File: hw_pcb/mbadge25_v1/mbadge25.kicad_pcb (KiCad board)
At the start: 2 copper layers, 8 parts, among them J1 USB4105-GF-A, U1 ESP32-C3-MINI-1

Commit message: v1 draft PCB layout
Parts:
- added C3: 100nF, Library_FP_mbadge25:C_1206_3216Metric_Pad1.33x1.80mm, F.Cu at (112.5, 83.2)
- added C4: 2.2µF, Library_FP_mbadge25:C_1206_3216Metric_Pad1.33x1.80mm, F.Cu at (103.2, 76.0)
- added C5: 2.2µF, Library_FP_mbadge25:C_1206_3216Metric_Pad1.33x1.80mm, F.Cu at (103.2, 78.8)
- added C6: 2.2µF, Library_FP_mbadge25:C_1206_3216Metric_Pad1.33x1.80mm, F.Cu at (112.7, 76.5)
- added C7: 100nF, Library_FP_mbadge25:C_1206_3216Metric_Pad1.33x1.80mm, F.Cu at (122.5, 86.5)
- added C8: 1µF, Library_FP_mbadge25:C_1206_3216Metric_Pad1.33x1.80mm, F.Cu at (77.5, 86.5)
- added C9: 1µF, Library_FP_mbadge25:C_1206_3216Metric_Pad1.33x1.80mm, F.Cu at (99.8, 88.5)
- added J2: BAT, Library_FP_mbadge25:PinHeader_1x02_P2.54mm_Vertical, F.Cu at (79.7, 53.0)
- added J3: OLED_I2C, Library_FP_mbadge25:OLED_128x32, F.Cu at (100.0, 82.0)
- added J4: BAT, Library_FP_mbadge25:Pad_6.0mm_Drill3.0mm, F.Cu at (76.0, 48.0)
- added J5: GND, Library_FP_mbadge25:Pad_6.0mm_Drill3.0mm, F.Cu at (124.0, 48.0)
- added J6: BAT, Library_FP_mbadge25:Pad_1.2mm_Drill0.7mm, F.Cu at (76.0, 53.0)
- added J7: GND, Library_FP_mbadge25:Pad_1.2mm_Drill0.7mm, F.Cu at (124.0, 53.0)
- added R2: 5k1, Library_FP_mbadge25:R_1206_3216Metric_Pad1.30x1.75mm, F.Cu at (116.0, 88.5)
- added R3: 27E, Library_FP_mbadge25:R_1206_3216Metric_Pad1.30x1.75mm, F.Cu at (108.0, 88.5)
- added R4: 27E, Library_FP_mbadge25:R_1206_3216Metric_Pad1.30x1.75mm, F.Cu at (110.5, 88.5)
- added R5: 100k, Library_FP_mbadge25:R_1206_3216Metric_Pad1.30x1.75mm, F.Cu at (112.5, 80.5)
- added R6: 100k, Library_FP_mbadge25:R_1206_3216Metric_Pad1.30x1.75mm, F.Cu at (122.5, 83.8)
- added R7: 10k, Library_FP_mbadge25:R_1206_3216Metric_Pad1.30x1.75mm, F.Cu at (77.5, 83.8)
- added R8: 220E, Library_FP_mbadge25:R_1206_3216Metric_Pad1.30x1.75mm, F.Cu at (122.5, 81.0)
- added S2: RST, Library_FP_mbadge25:SW_SPST, F.Cu at (77.5, 94.0)
- added T1: LP0404N3T5G, Library_FP_mbadge25:SOT-23-3, F.Cu at (103.5, 82.5)
- added U2: XC6220B331MR, Library_FP_mbadge25:SOT-23-5_HandSoldering, F.Cu at (108.7, 77.2)
- C1: value C -> 47pF; footprint PCM_Capacitor_SMD_AKL:C_0805_2012Metric_Pad1.18x1.45mm_HandSolder -> Library_FP_mbadge25:C_1206_3216Metric_Pad1.33x1.80mm
- C2: value C-polar -> 47pF; footprint PCM_Capacitor_SMD_AKL:CP_Elec_6.3x5.9 -> Library_FP_mbadge25:C_1206_3216Metric_Pad1.33x1.80mm
- D1: value type="" model="D" lib="semiconductor.lib" -> MSK4005; footprint Diode_SMD:D_SOD-123 -> Library_FP_mbadge25:D_SOD-523
- D2: value type="" model="D-LED" lib="semiconductor.lib" -> WS2812B; footprint Diode_SMD:D_SMA -> Library_FP_mbadge25:LED_WS2812B_PLCC4_5.0x5.0mm_P3.2mm
- R1: value R -> 5k1; footprint Resistor_SMD:R_0805_2012Metric -> Library_FP_mbadge25:R_1206_3216Metric_Pad1.30x1.75mm
- S1: value S-make-push -> SW; footprint Button_Switch_THT:SW_PUSH_6mm -> Library_FP_mbadge25:SW_SPST
- U1: footprint PCM_Espressif:ESP32-C3-MINI-1 -> Library_FP_mbadge25:ESP32-C3-MINI-1
- moved S1 86.3 mm to (122.5, 94.0), turned to 90 degrees
- moved J1 78.0 mm to (109.2, 97.2)
- moved C2 71.9 mm to (105.2, 88.5), turned to -90 degrees
- moved D2 70.6 mm to (122.5, 76.0), turned to -90 degrees
- moved U1 69.6 mm to (91.1, 91.5), turned to 180 degrees
- moved C1 66.2 mm to (113.2, 88.5), turned to -90 degrees
- moved D1 58.9 mm to (108.0, 80.8)
- moved R1 54.8 mm to (102.5, 88.5), turned to 90 degrees
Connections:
- C1 pad 1: unconnected-(C1-+-Pad1) -> /IO18.USBN
- C1 pad 2: unconnected-(C1---Pad2) -> /GND
- C2 pad 1: unconnected-(C2-+-Pad1) -> /IO19.USBP
- C2 pad 2: unconnected-(C2---Pad2) -> /GND
- D1 pad 1: unconnected-(D1-K--Pad1) -> /5V0
- D1 pad 2: unconnected-(D1-A+-Pad2) -> /VUSB
- D2 pad 1: unconnected-(D2-K--Pad1) -> /5V0
- D2 pad 2: unconnected-(D2-A+-Pad2) -> /RGB.DO
- J1 pad A1_B12: unconnected-(J1-GND-PadA1_B12) -> /GND
- J1 pad A4_B9: unconnected-(J1-VBUS-PadA4_B9) -> /VUSB
- J1 pad A5: unconnected-(J1-CC1-PadA5) -> Net-(J1-CC1)
- J1 pad A6: unconnected-(J1-DP1-PadA6) -> /DP
- J1 pad A7: unconnected-(J1-DN1-PadA7) -> /DN
- J1 pad B1_A12: unconnected-(J1-GND__1-PadB1_A12) -> /GND
- J1 pad B4_A9: unconnected-(J1-VBUS__1-PadB4_A9) -> /VUSB
- J1 pad B5: unconnected-(J1-CC2-PadB5) -> Net-(J1-CC2)
- J1 pad B6: unconnected-(J1-DP2-PadB6) -> /DP
- J1 pad B7: unconnected-(J1-DN2-PadB7) -> /DN
- J1 pad SH1: unconnected-(J1-SHELL_GND-PadSH1) -> /GND
- J1 pad SH2: unconnected-(J1-SHELL_GND__1-PadSH2) -> /GND
- J1 pad SH3: unconnected-(J1-SHELL_GND__2-PadSH3) -> /GND
- J1 pad SH4: unconnected-(J1-SHELL_GND__3-PadSH4) -> /GND
- R1 pad 1: unconnected-(R1-+-Pad1) -> Net-(J1-CC1)
- R1 pad 2: unconnected-(R1---Pad2) -> /GND
- S1 pad 1: (no net) -> /IO9
- S1 pad 2: (no net) -> /GND
- U1 pad 1: Net-(U1-GND-Pad1) -> /GND
- U1 pad 11: Net-(U1-GND-Pad1) -> /GND
- U1 pad 14: Net-(U1-GND-Pad1) -> /GND
- U1 pad 16: unconnected-(U1-GPIO10-Pad16) -> /IO10
- U1 pad 18: unconnected-(U1-GPIO4/ADC1_CH4-Pad18) -> /IO4
- U1 pad 19: unconnected-(U1-GPIO5/ADC2_CH0-Pad19) -> /IO5
- U1 pad 2: Net-(U1-GND-Pad1) -> /GND
- U1 pad 20: unconnected-(U1-GPIO6-Pad20) -> /IO6.RGB
- U1 pad 21: unconnected-(U1-GPIO7-Pad21) -> /IO7.SDA
- U1 pad 22: unconnected-(U1-GPIO8-Pad22) -> /IO8.SCL
- U1 pad 23: unconnected-(U1-GPIO9-Pad23) -> /IO9
- U1 pad 26: unconnected-(U1-GPIO18/USB_D--Pad26) -> /IO18.USBN
- U1 pad 27: unconnected-(U1-GPIO19/USB_D+-Pad27) -> /IO19.USBP
- U1 pad 3: unconnected-(U1-3V3-Pad3) -> /3V3
- U1 pad 30: unconnected-(U1-GPIO20/U0RXD-Pad30) -> /IO20.RX
- U1 pad 31: unconnected-(U1-GPIO21/U0TXD-Pad31) -> /IO21.TX
- U1 pad 36: Net-(U1-GND-Pad1) -> /GND
- U1 pad 37: Net-(U1-GND-Pad1) -> /GND
- U1 pad 38: Net-(U1-GND-Pad1) -> /GND
- U1 pad 39: Net-(U1-GND-Pad1) -> /GND
- U1 pad 40: Net-(U1-GND-Pad1) -> /GND
- U1 pad 41: Net-(U1-GND-Pad1) -> /GND
- U1 pad 42: Net-(U1-GND-Pad1) -> /GND
- U1 pad 43: Net-(U1-GND-Pad1) -> /GND
- U1 pad 44: Net-(U1-GND-Pad1) -> /GND
- U1 pad 45: Net-(U1-GND-Pad1) -> /GND
- U1 pad 46: Net-(U1-GND-Pad1) -> /GND
- U1 pad 47: Net-(U1-GND-Pad1) -> /GND
- U1 pad 48: Net-(U1-GND-Pad1) -> /GND
- U1 pad 49: Net-(U1-GND-Pad1) -> /GND
- U1 pad 5: unconnected-(U1-GPIO2/ADC1_CH2-Pad5) -> /IO2
- U1 pad 50: Net-(U1-GND-Pad1) -> /GND
- U1 pad 51: Net-(U1-GND-Pad1) -> /GND
- U1 pad 52: Net-(U1-GND-Pad1) -> /GND
- U1 pad 53: Net-(U1-GND-Pad1) -> /GND
- U1 pad 6: unconnected-(U1-GPIO3/ADC1_CH3-Pad6) -> /IO3
- U1 pad 8: unconnected-(U1-EN/CHIP_PU-Pad8) -> Net-(C8-+)
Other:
- board outline added: 55.5 x 57.2 mm
- board text added: "[+]"
- board text added: "[-]"

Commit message: v2 draft PCB layout
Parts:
- removed D2: WS2812B, Library_FP_mbadge25:LED_WS2812B_PLCC4_5.0x5.0mm_P3.2mm
- removed J4: BAT, Library_FP_mbadge25:Pad_6.0mm_Drill3.0mm
- removed J5: GND, Library_FP_mbadge25:Pad_6.0mm_Drill3.0mm
- removed J6: BAT, Library_FP_mbadge25:Pad_1.2mm_Drill0.7mm
- removed J7: GND, Library_FP_mbadge25:Pad_1.2mm_Drill0.7mm
- removed R8: 220E, Library_FP_mbadge25:R_1206_3216Metric_Pad1.30x1.75mm
- added J10: Conn_IO20.RX, Library_FP_mbadge25:PinHeader_1x01_P1.27mm_Vertical, F.Cu at (110.8, 78.1)
- added J11: Conn_IO19.USBP, Library_FP_mbadge25:PinHeader_1x01_P1.27mm_Vertical, F.Cu at (109.5, 78.1)
- added J12: Conn_IO18.USBN, Library_FP_mbadge25:PinHeader_1x01_P1.27mm_Vertical, F.Cu at (108.3, 78.1)
- added J13: Conn_IO2, Library_FP_mbadge25:PinHeader_1x01_P1.27mm_Vertical, F.Cu at (112.1, 62.2)
- added J14: Conn_IO3, Library_FP_mbadge25:PinHeader_1x01_P1.27mm_Vertical, F.Cu at (110.8, 62.2)
- added J15: Conn_IO4, Library_FP_mbadge25:PinHeader_1x01_P1.27mm_Vertical, F.Cu at (103.8, 68.5)
- added J16: Conn_IO5, Library_FP_mbadge25:PinHeader_1x01_P1.27mm_Vertical, F.Cu at (103.8, 69.8)
- added J17: Conn_IO6.RGB, Library_FP_mbadge25:PinHeader_1x01_P1.27mm_Vertical, F.Cu at (103.8, 71.1)
- added J18: Conn_IO7.SDA, Library_FP_mbadge25:PinHeader_1x01_P1.27mm_Vertical, F.Cu at (103.8, 72.4)
- added J19: Conn_IO8.SCL, Library_FP_mbadge25:PinHeader_1x01_P1.27mm_Vertical, F.Cu at (103.8, 73.6)
- added J20: Conn_IO10, Library_FP_mbadge25:PinHeader_1x01_P1.27mm_Vertical, F.Cu at (103.8, 67.3)
- added J21: Conn_IO00, Library_FP_mbadge25:PinHeader_1x01_P1.27mm_Vertical, F.Cu at (103.8, 64.7)
- added J22: Conn_IO01, Library_FP_mbadge25:PinHeader_1x01_P1.27mm_Vertical, F.Cu at (103.8, 66.0)
- added J8: USB-C_BO, Library_FP_mbadge25:USB_C_BO, F.Cu at (100.0, 88.4)
- added J9: Conn_IO21.TX, Library_FP_mbadge25:PinHeader_1x01_P1.27mm_Vertical, F.Cu at (112.1, 78.1)
- moved U1 31.2 mm to (114.0, 70.2), turned to -90 degrees
- moved R5 30.3 mm to (83.4, 71.9), turned to 90 degrees
- moved J2 29.6 mm to (81.6, 82.5), turned to 180 degrees
- moved C6 27.0 mm to (86.1, 71.9)
- moved D1 20.9 mm to (90.1, 69.8), turned to 180 degrees
- moved T1 20.4 mm to (90.1, 67.1), turned to 0 degrees
- moved U2 19.2 mm to (90.1, 72.6), turned to 180 degrees
- moved C3 18.8 mm to (93.7, 82.7), turned to 90 degrees
- moved C9 16.6 mm to (99.8, 71.9), turned to -90 degrees
- moved C1 15.6 mm to (98.7, 82.7)
- moved C8 14.1 mm to (91.1, 82.7), turned to 90 degrees
- moved J3 11.9 mm to (97.2, 70.5)
- moved R6 11.1 mm to (111.4, 82.7), turned to 90 degrees
- moved R7 11.1 mm to (88.6, 82.7), turned to 90 degrees
- moved R4 10.9 mm to (101.3, 82.7)
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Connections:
- net /IO9 renamed /IO9.SW
- net Net-(C8-+) renamed /EN
- net Net-(J1-CC1) renamed /CC1
- net Net-(J1-CC2) renamed /CC2
- J1 pad A8: unconnected-(J1-SBU1-PadA8) -> /SBU1
- J1 pad B8: unconnected-(J1-SBU2-PadB8) -> /SBU2
- U1 pad 12: unconnected-(U1-GPIO0/ADC1_CH0/XTAL_32K_P-Pad12) -> Net-(J21-Pin_1)
- U1 pad 13: unconnected-(U1-GPIO1/ADC1_CH1/XTAL_32K_N-Pad13) -> Net-(J22-Pin_1)
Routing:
- net /GND: track 0.00 -> 153.4 mm, vias 0 -> 19
- net /3V3: track 0.00 -> 79.8 mm, vias 0 -> 4
- net /EN: track 0.00 -> 64.0 mm, vias 0 -> 2
- net /VUSB: track 0.00 -> 63.8 mm, vias 0 -> 1
- net /IO9.SW: track 0.00 -> 42.1 mm, vias 0 -> 2
- net /IO8.SCL: track 0.00 -> 33.9 mm
- net /IO7.SDA: track 0.00 -> 33.0 mm
- net /VBAT: track 0.00 -> 23.1 mm, vias 0 -> 1
- net /CC2: track 0.00 -> 14.5 mm
- net /IO18.USBN: track 0.00 -> 14.2 mm
- net /5V0: track 0.00 -> 13.6 mm
- net /DP: track 0.00 -> 12.9 mm
- net /IO19.USBP: track 0.00 -> 12.9 mm
- net /DN: track 0.00 -> 11.8 mm
- net /CC1: track 0.00 -> 9.26 mm
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- added copper zone on B.Cu, net /GND
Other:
- board size 55.5 x 57.2 mm -> 44 x 44 mm

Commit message: draft PCB layout WIP
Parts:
- removed J13: Conn_IO2, Library_FP_mbadge25:PinHeader_1x01_P1.27mm_Vertical
- removed J14: Conn_IO3, Library_FP_mbadge25:PinHeader_1x01_P1.27mm_Vertical
- added D2: WS2812B, Library_FP_mbadge25:LED_WS2812B_PLCC4_5.0x5.0mm_P3.2mm, B.Cu at (100.0, 78.0)
- added J23: RGB, Library_FP_mbadge25:PinSocket_1x03_P1.27mm_Vertical, F.Cu at (86.0, 58.2)
- added J24: Simple_Addon_v2, Library_FP_mbadge25:PinSocket_2x03_P2.54mm_Vertical, F.Cu at (109.7, 58.1)
- added R8: 220E, Library_FP_mbadge25:R_1206_3216Metric_Pad1.30x1.75mm, F.Cu at (100.0, 78.0)
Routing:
- net /3V3: track 79.8 -> 76.7 mm
- net /IO3: track 2.31 -> 0.00 mm
- net /IO2: track 2.12 -> 0.00 mm
- net /IO18.USBN: track 14.2 -> 13.6 mm
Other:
- board text removed: "[+]"
- board text removed: "[-]"

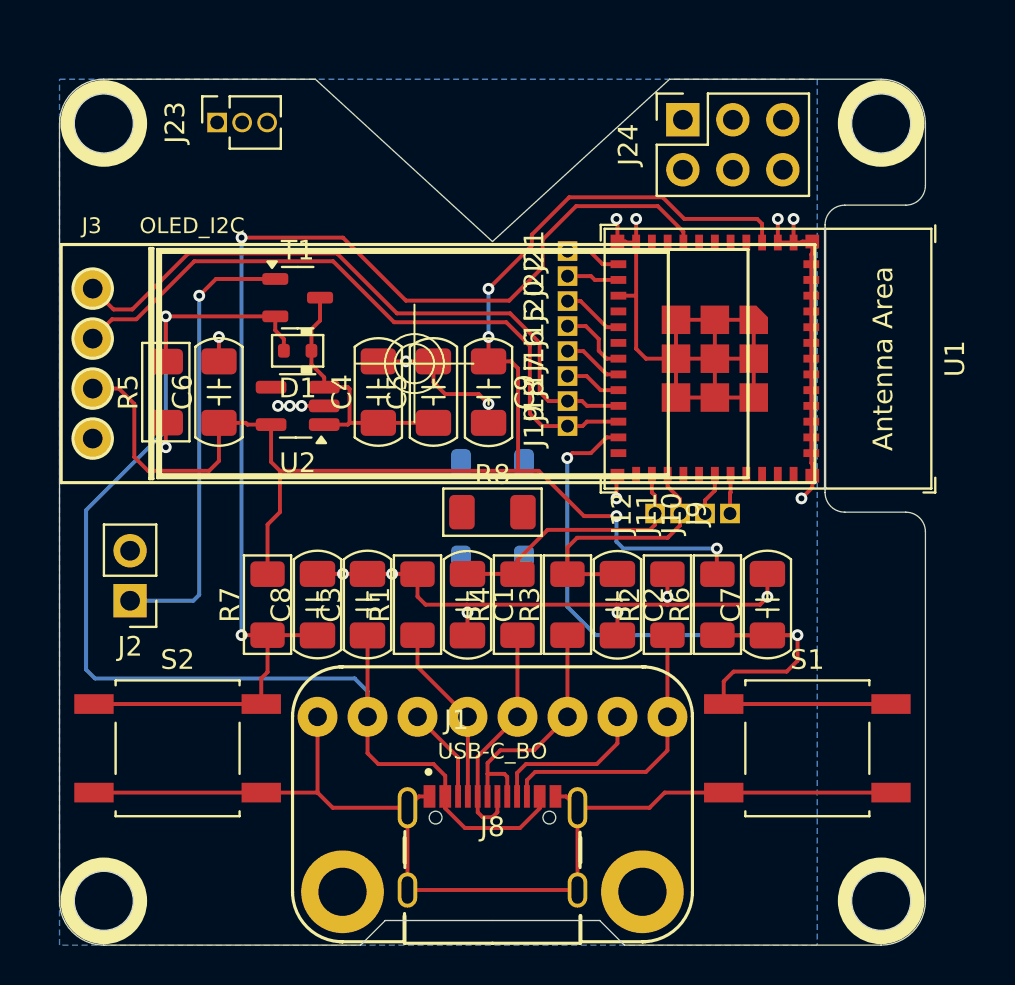
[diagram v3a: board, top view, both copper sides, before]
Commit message: changed PCB dims, rearranged components
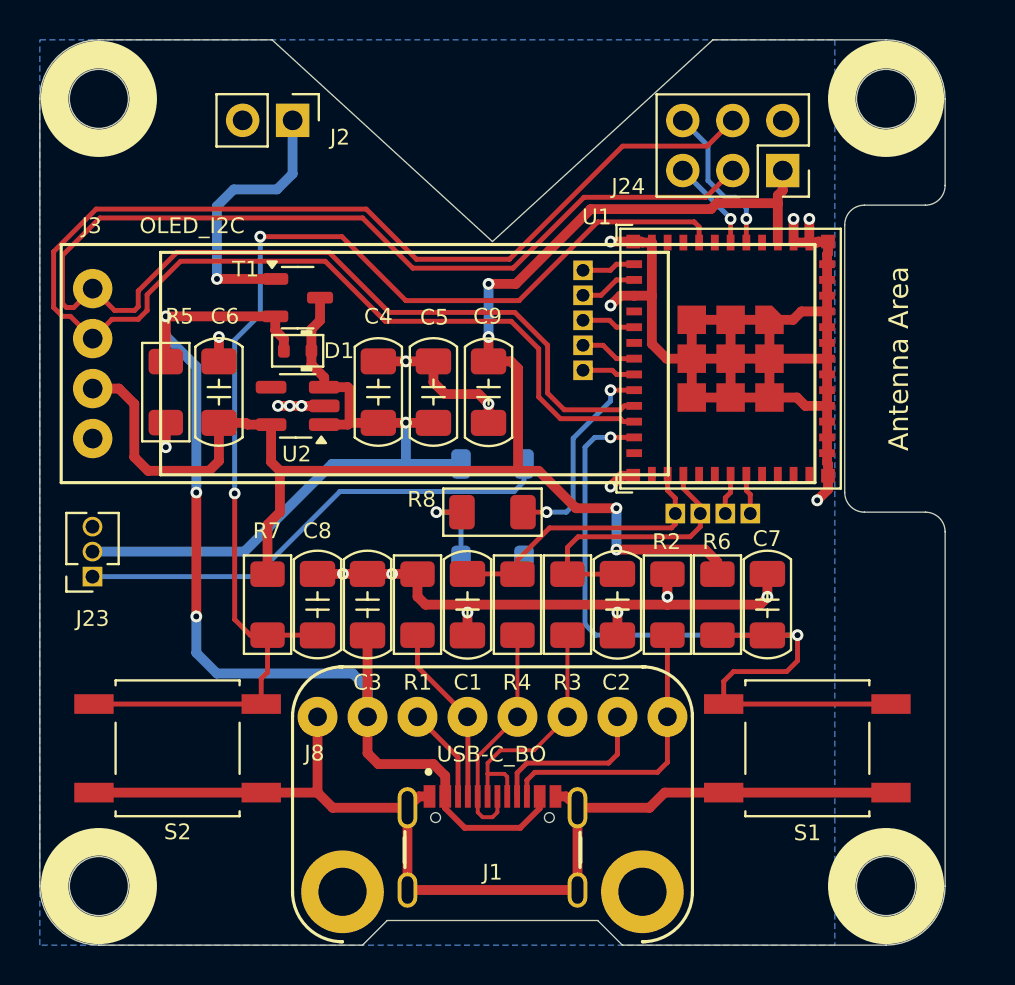
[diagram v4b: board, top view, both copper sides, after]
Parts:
- removed J17: Conn_IO6.RGB, Library_FP_mbadge25:PinHeader_1x01_P1.27mm_Vertical
- removed J18: Conn_IO7.SDA, Library_FP_mbadge25:PinHeader_1x01_P1.27mm_Vertical
- removed J19: Conn_IO8.SCL, Library_FP_mbadge25:PinHeader_1x01_P1.27mm_Vertical
- moved J2 25.8 mm to (89.8, 58.1), turned to -90 degrees
- moved J23 23.9 mm to (79.7, 81.3), turned to 180 degrees
- moved J24 5.69 mm to (114.8, 60.6), turned to -90 degrees
- moved J16 1.25 mm to (104.6, 70.8)
- moved J22 1.25 mm to (104.6, 67.0)
- moved J15 1.25 mm to (104.6, 69.5)
- moved J20 1.25 mm to (104.6, 68.2)
- moved J21 1.25 mm to (104.6, 65.7)
- moved J10 1.03 mm to (111.8, 78.1)
- moved J11 1.03 mm to (110.6, 78.1)
- moved J12 1.03 mm to (109.3, 78.1)
- moved J9 1.03 mm to (113.1, 78.1)
- moved U1 0.80 mm to (114.8, 70.2)
- turned D2 to -90 degrees
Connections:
- net /IO2 renamed /IO2.SAO
- net /IO3 renamed /IO3.SAO
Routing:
- net /IO8.SCL: track 33.9 -> 79.3 mm
- net /IO7.SDA: track 33.0 -> 76.9 mm
- net /RGB.DO: track 0.00 -> 24.8 mm
- net /5V0: track 13.6 -> 36.3 mm, vias 0 -> 1
- net /GND: track 153.4 -> 162.9 mm
- net /VBAT: track 23.1 -> 13.9 mm
- net /IO2.SAO: track 0.00 -> 7.86 mm, vias 0 -> 1
- net /IO6.RGB: track 2.88 -> 10.5 mm, vias 0 -> 2
- net /VUSB: track 63.8 -> 56.7 mm, vias 1 -> 3
- net /RGB.DI: track 0.00 -> 4.71 mm, vias 0 -> 1
- net /IO3.SAO: track 0.00 -> 4.67 mm, vias 0 -> 1
- net /3V3: track 76.7 -> 79.9 mm
- net /IO19.USBP: track 12.9 -> 14.1 mm
- net /IO18.USBN: track 13.6 -> 14.7 mm
- net /EN: track 63.9 -> 62.9 mm
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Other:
- board size 44 x 44 mm -> 46 x 46 mm
